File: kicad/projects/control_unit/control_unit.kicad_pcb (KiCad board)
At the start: 2 copper layers, 177.8 x 76.2 mm, 30 parts, among them J1 BUS, J2 FLAGS, J3 INSTRUCTION, J4 BACKPLANE, J5 MIR INST LEDS, J6 STEP LEDS, J7 MIR FLAG LEDS, J8 STEP RESET, J9 MASTER RESET, U1 28C256, U2 28C256, U3 28C256, U4 28C256, U5 74HCT377, U6 74HCT161, U7 74HCT173, U8 74HCT138, U9 74HCT04

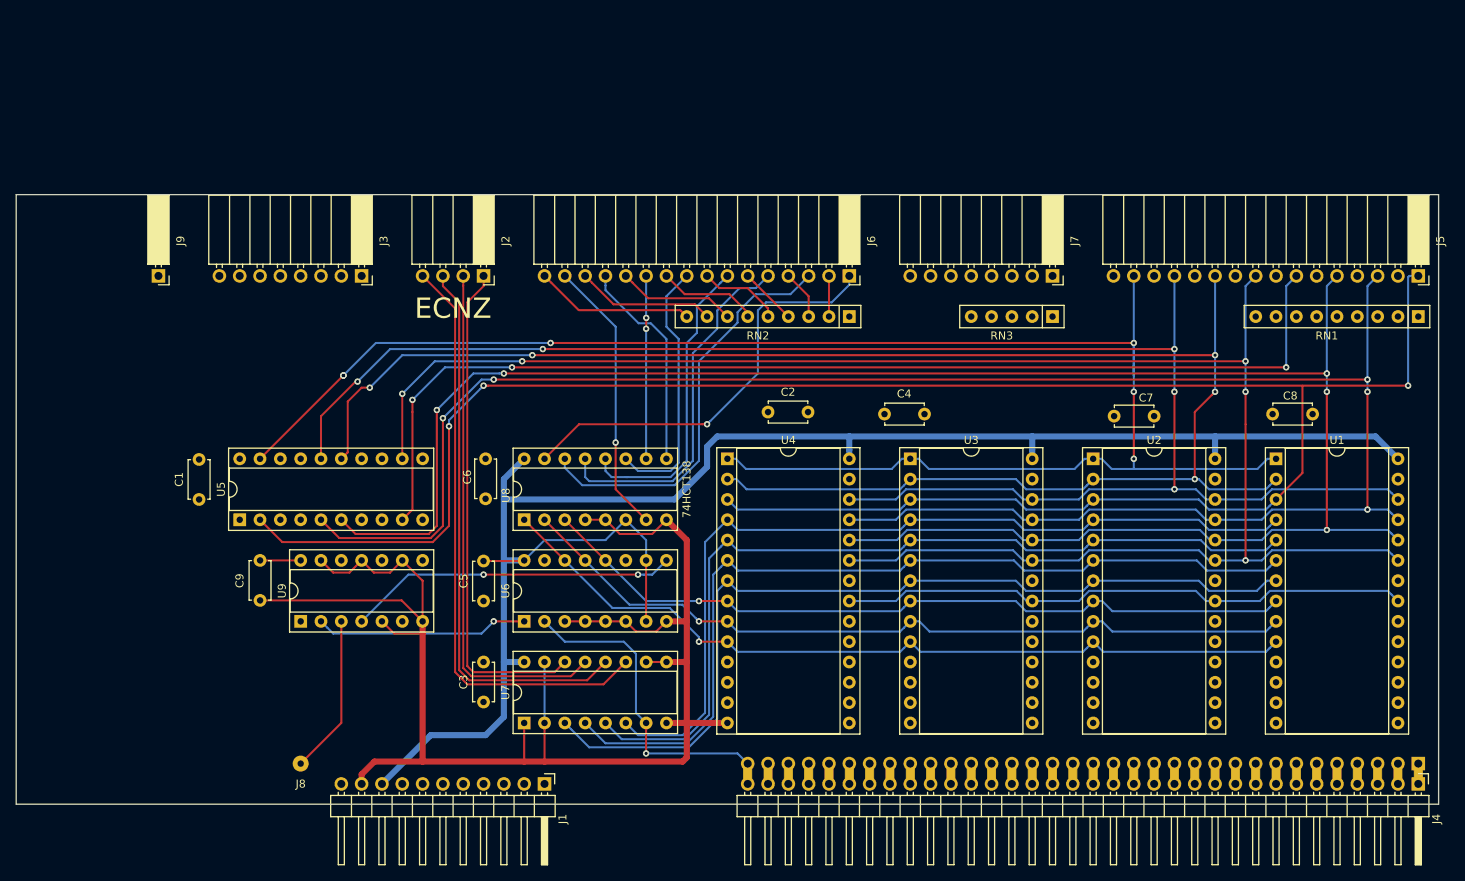
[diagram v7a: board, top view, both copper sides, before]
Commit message: Finish control unit PCB
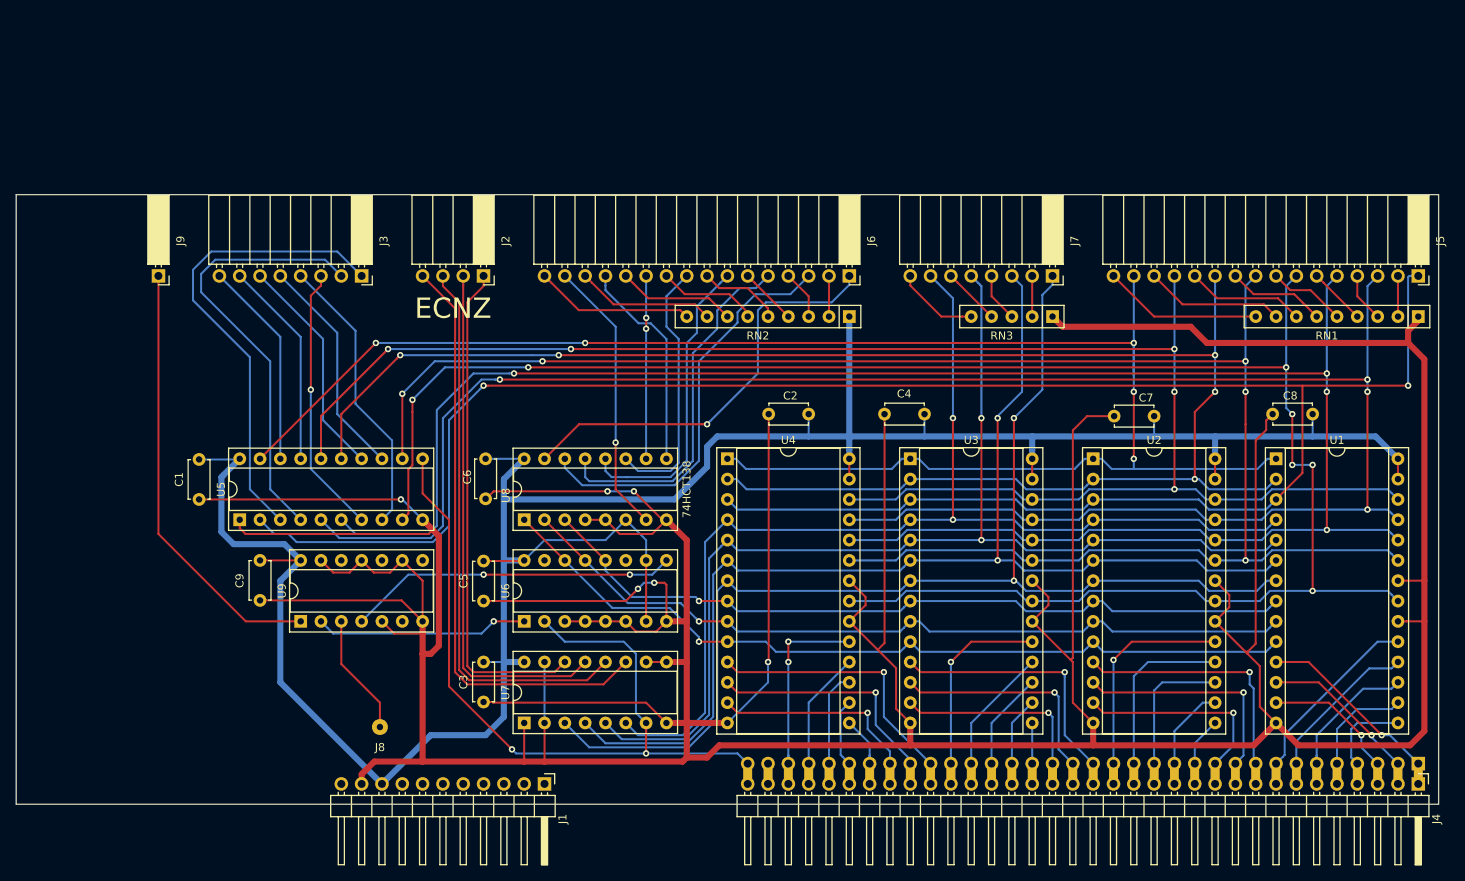
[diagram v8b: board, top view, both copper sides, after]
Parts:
- moved J8 10.9 mm to (91.2, 109.7)
- moved C2 5.09 mm to (144.8, 70.6), turned to 180 degrees
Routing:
- net GND: track 197.4 -> 759.5 mm, vias 0 -> 6
- net VCC: track 221.9 -> 326.2 mm
- net /CONTROL_CLOCK: track 39.3 -> 99.8 mm, vias 1 -> 2
- net Net-(J3-Pad1): track 0.00 -> 59.1 mm
- net Net-(J3-Pad2): track 0.00 -> 55.2 mm
- net Net-(J9-Pad1): track 0.00 -> 54.6 mm
- net /MIR_FLAG_Z: track 111.3 -> 151.4 mm, vias 0 -> 2
- net /MIR_FLAG_N: track 110.5 -> 147.8 mm, vias 0 -> 2
- net /ROM_3_0: track 0.00 -> 36.5 mm, vias 0 -> 1
- net Net-(J3-Pad4): track 0.00 -> 35.7 mm
- net /ROM_2_0: track 0.00 -> 35.3 mm, vias 0 -> 1
- net /ROM_1_0: track 0.00 -> 34.4 mm, vias 0 -> 1
- net Net-(J3-Pad3): track 0.00 -> 33.6 mm, vias 0 -> 1
- net /MIR_FLAG_C: track 109.6 -> 143.1 mm, vias 0 -> 2
- net /ROM_3_1: track 0.00 -> 32.3 mm, vias 0 -> 1
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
